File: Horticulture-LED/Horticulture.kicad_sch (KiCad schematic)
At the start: 61 parts, among them J3 Conn_01x04_Male, J4 Conn_01x04_Male, U1 TLE4309, U2 TLE4309, U3 TLE4309, U4 TLE4309, U5 PCA9633DP2, U6 MCP1703A-1502_SOT223

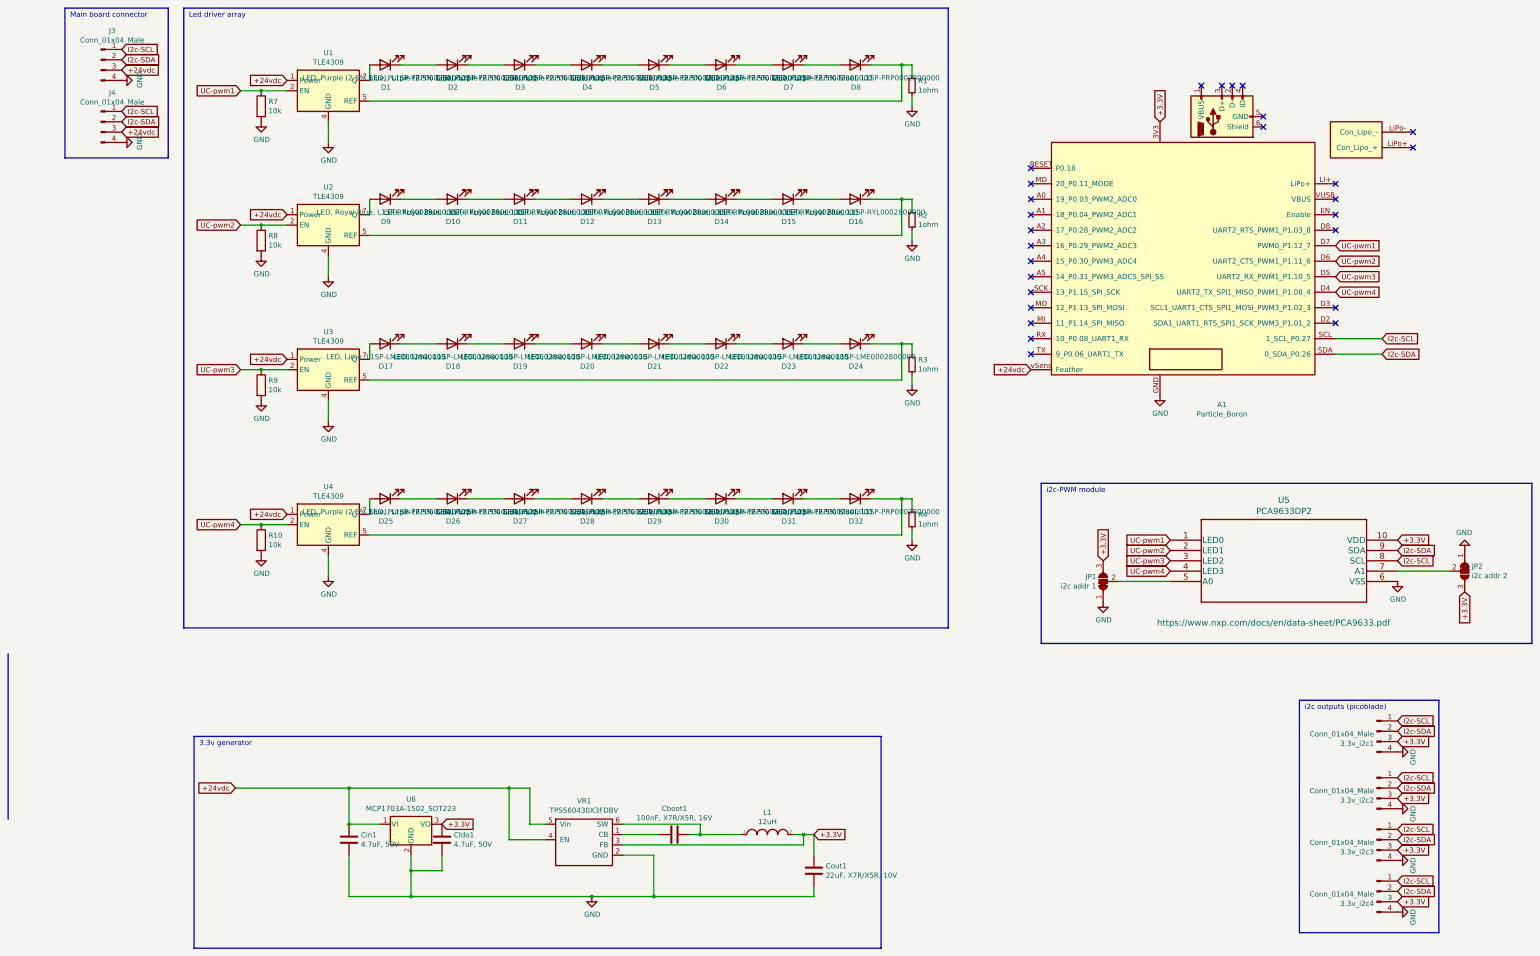
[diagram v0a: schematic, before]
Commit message: Updated to kicad 8
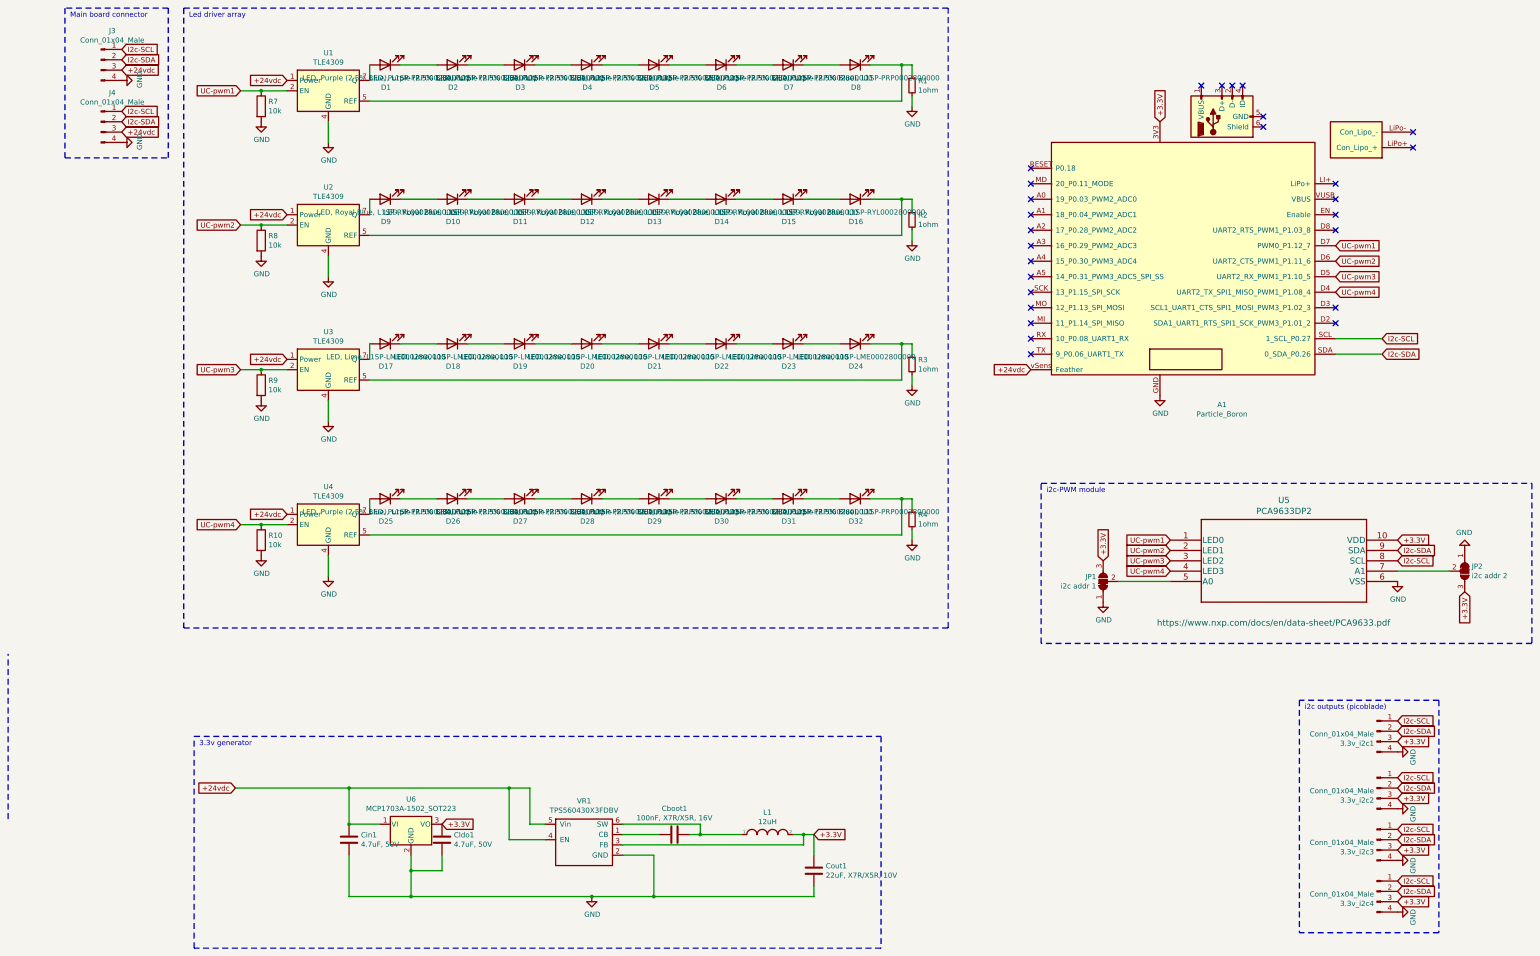
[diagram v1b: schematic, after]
